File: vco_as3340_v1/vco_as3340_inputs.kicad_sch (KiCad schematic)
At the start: 36 parts, among them J2 FREQ_CV, J3 SOFT_SYNC

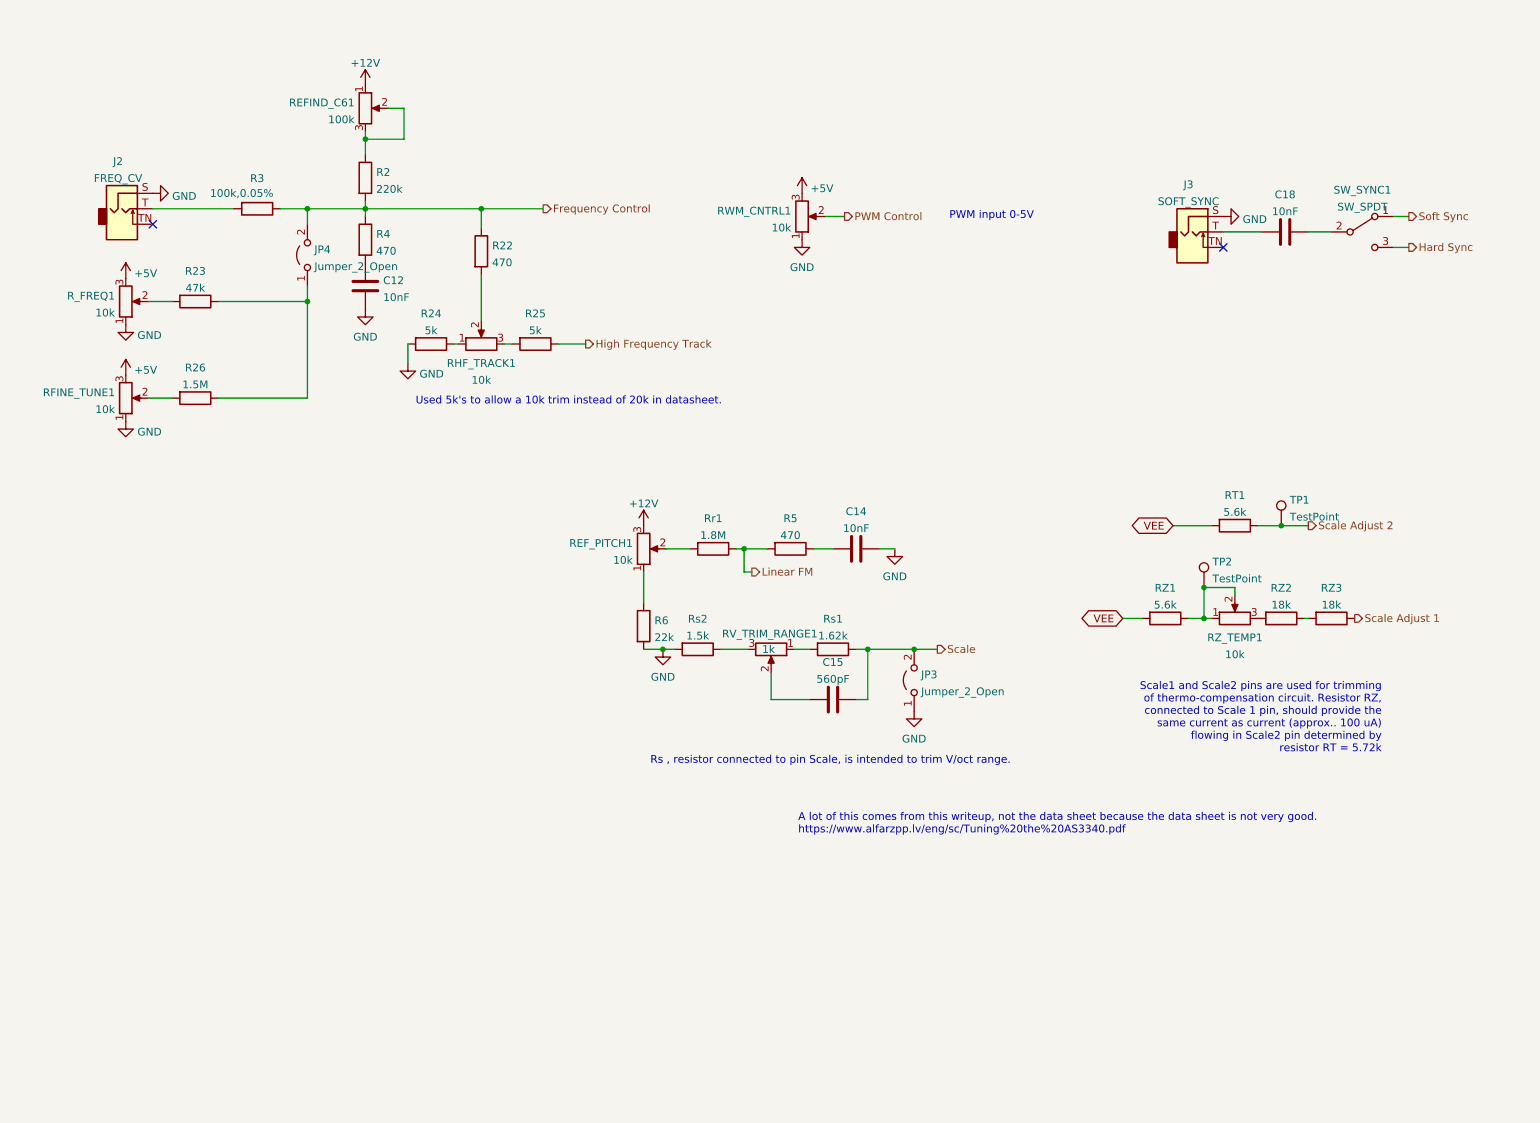
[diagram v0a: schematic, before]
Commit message: Schematic update from breadboarding, start layout
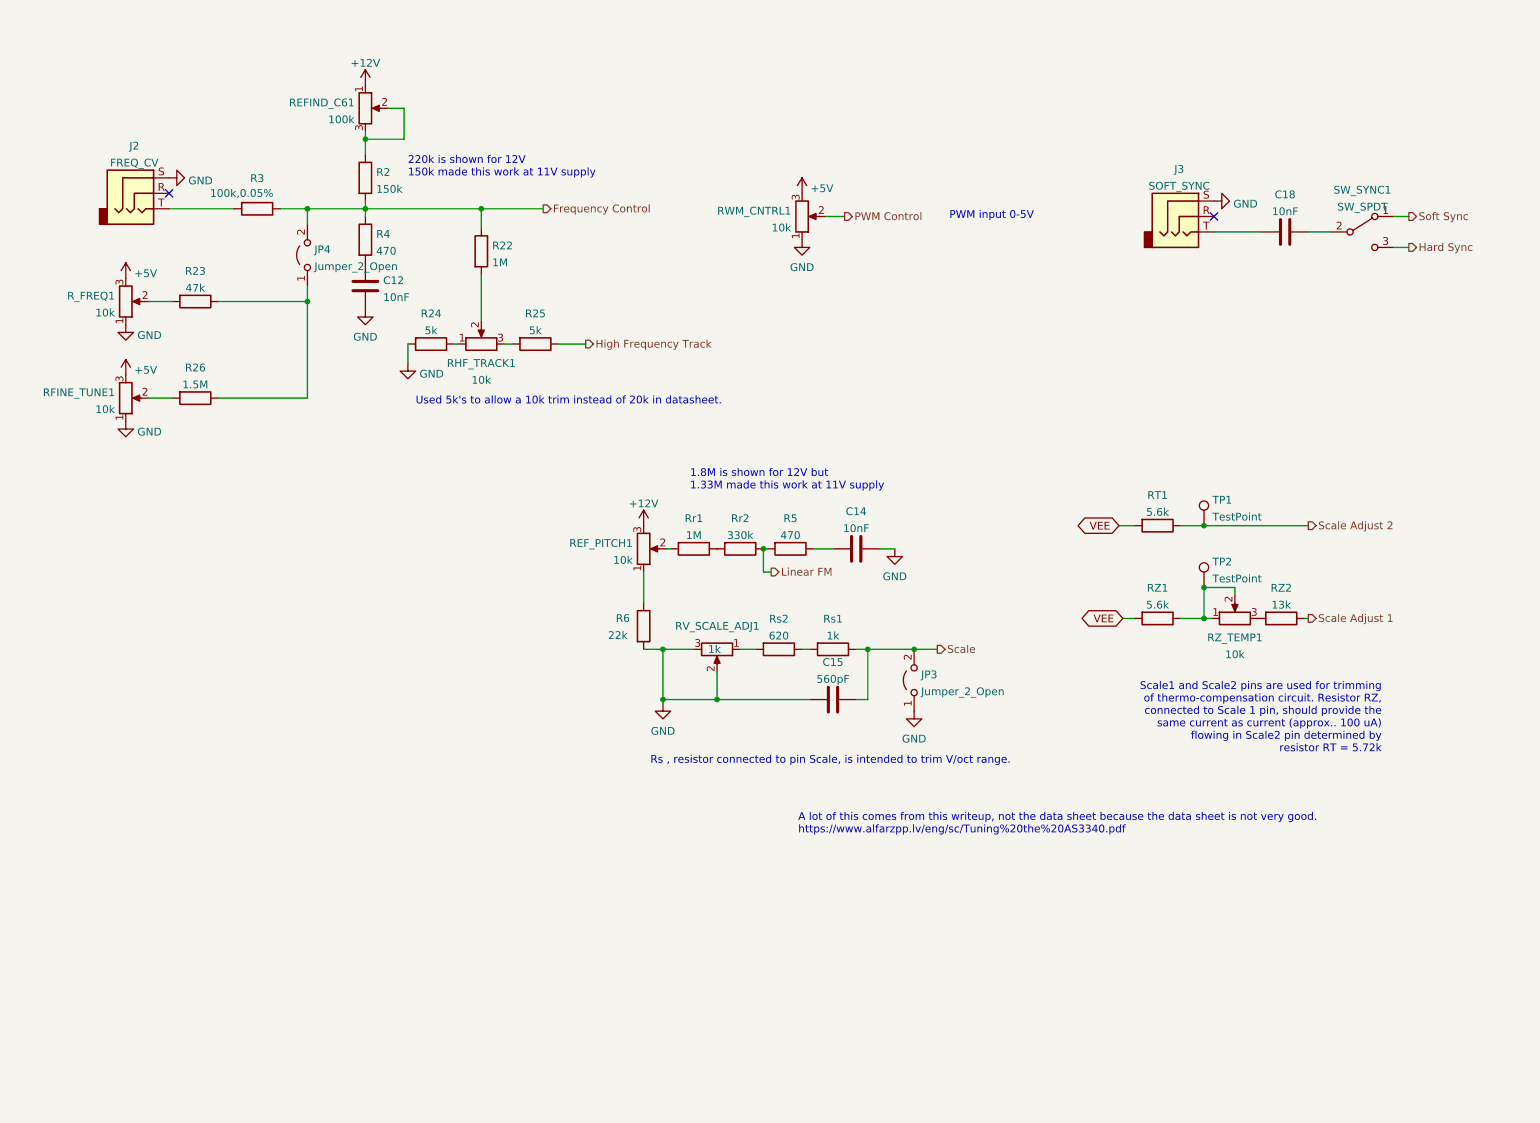
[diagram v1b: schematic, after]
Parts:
- removed RZ3: 18k, Resistor_SMD:R_1206_3216Metric_Pad1.30x1.75mm_HandSolder, symbol Device:R
- added Rr2: 330k, Resistor_SMD:R_1206_3216Metric_Pad1.30x1.75mm_HandSolder, symbol Device:R
- C12, C14, C15, C18: footprint Capacitor_THT:C_Disc_D6.0mm_W4.4mm_P5.00mm -> Capacitor_SMD:C_1206_3216Metric_Pad1.33x1.80mm_HandSolder
- J2, J3: symbol Connector:AudioJack2_SwitchT -> Connector:AudioJack3
- R2: value 220k -> 150k
- R22: value 470 -> 1M
- RZ2: value 18k -> 13k
- Rr1: value 1.8M -> 1M
- Rs1: value 1.62k -> 1k
- Rs2: value 1.5k -> 620
- renumbered RV_TRIM_RANGE1 to RV_SCALE_ADJ1
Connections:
- net GND: now also C15.1, RV_SCALE_ADJ1.2, RV_SCALE_ADJ1.3; no longer Rs2.2
- net Linear FM: now also Rr2.1; no longer Rr1.1
- net Scale Adjust 1: now also RZ2.1
- net at RV_SCALE_ADJ1.1: now also Rs2.2; no longer Rs1.2
- net at Rs2.1: now also Rs1.2; no longer RV_SCALE_ADJ1.3
- new net: Rr1.1, Rr2.2
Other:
- note added: "1.8M is shown for 12V but 1.33M made this work at 11V supply"
- note added: "220k is shown for 12V 150k made this work at 11V supply"
- moved on the sheet: RT1, RV_SCALE_ADJ1, RZ1, Rr1, TP1

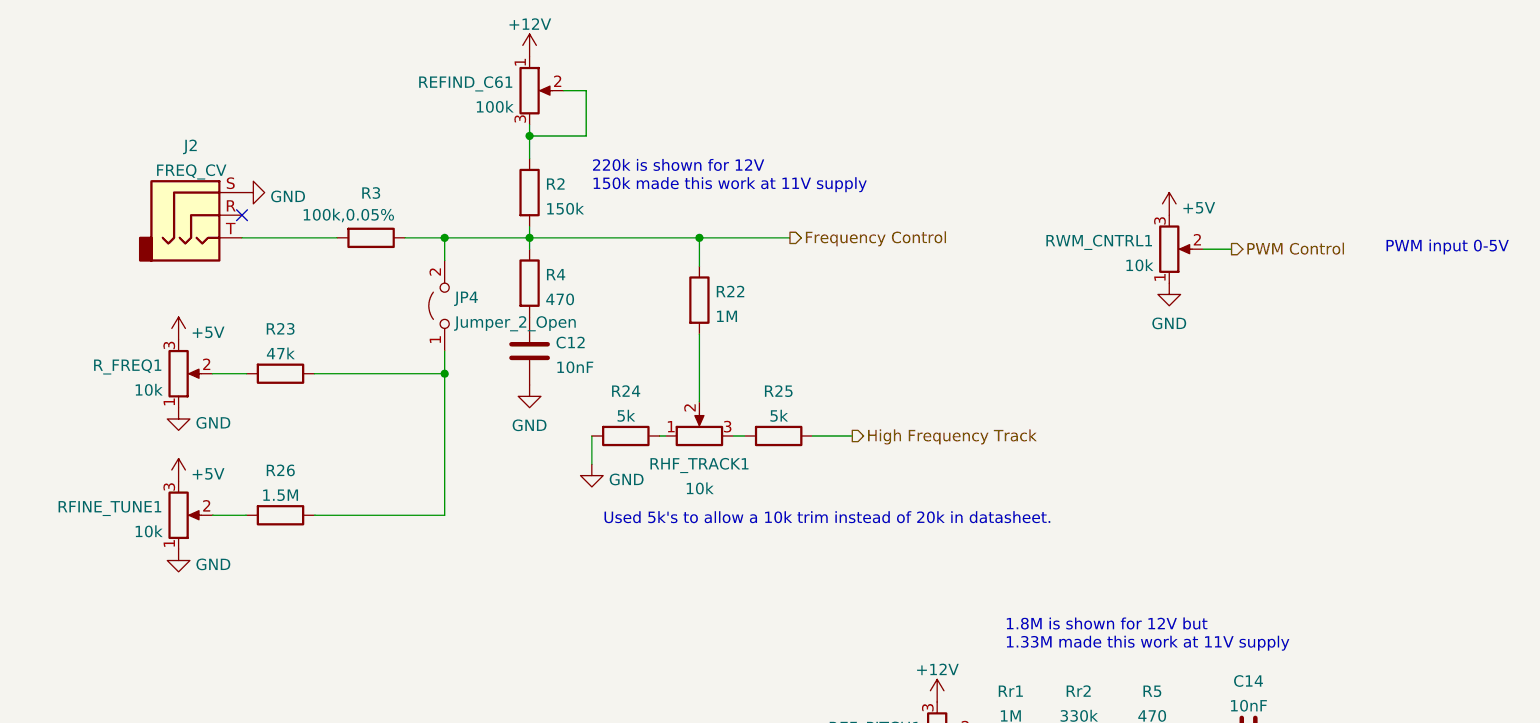
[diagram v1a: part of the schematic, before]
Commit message: Layout and routing done
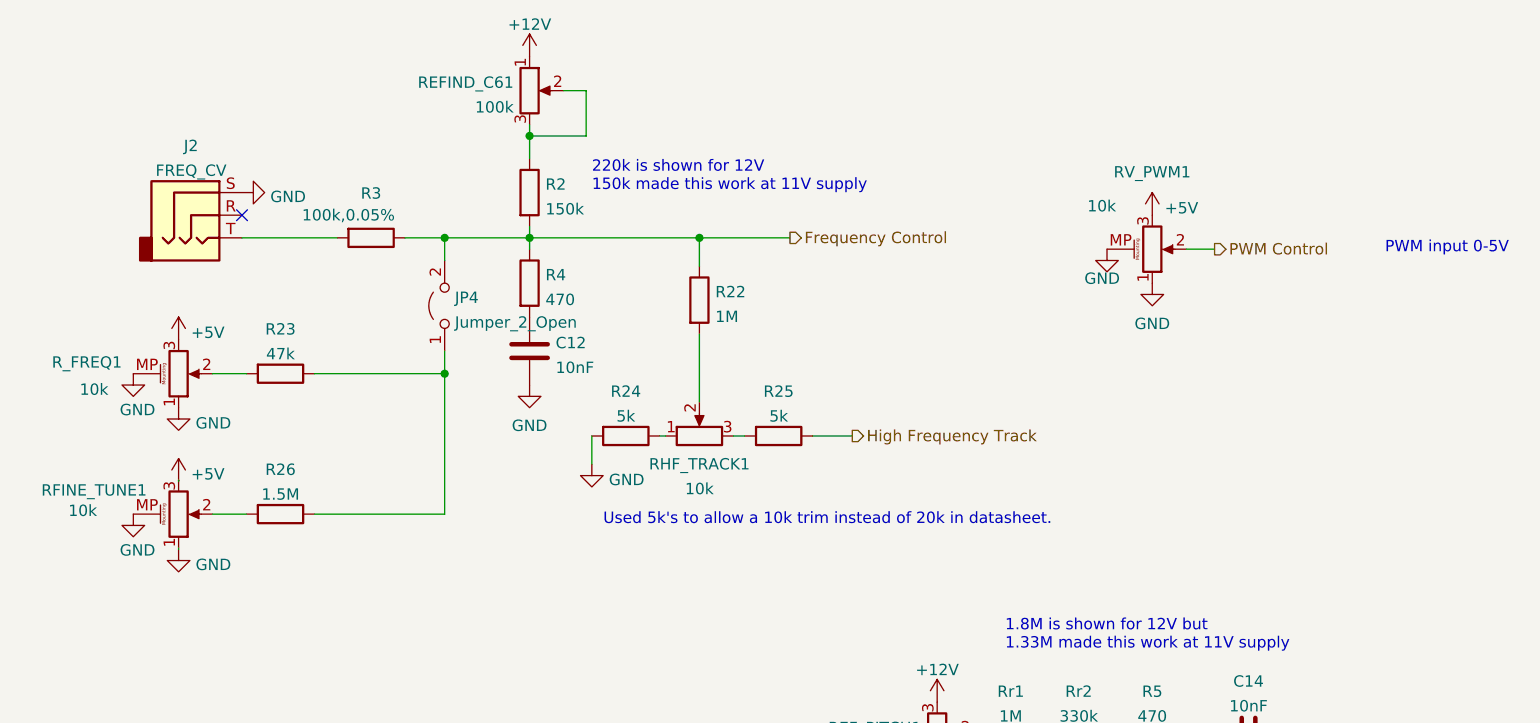
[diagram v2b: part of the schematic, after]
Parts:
- RFINE_TUNE1, R_FREQ1: symbol Device:R_Potentiometer -> Device:R_Potentiometer_MountingPin
- RV_PWM1: renamed from RWM_CNTRL1; symbol Device:R_Potentiometer -> Device:R_Potentiometer_MountingPin
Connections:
- net GND: now also RFINE_TUNE1.MP (MountPin), RV_PWM1.MP (MountPin), R_FREQ1.MP (MountPin)

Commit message: Geographic re-annotate and cleanup
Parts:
- J101: renamed from J3; value SOFT_SYNC -> SYNC
- renumbered C15 to C5, RHF_TRACK1 to HF_TRACK1, J2 to J100, JP4 to JP1, JP3 to JP4, R2 to R1, R5 to R12, R4 to R19, R23 to R2, R25 to R21, R24 to R23, R26 to R3, R3 to R30, R6 to R4, REFIND_C61 to REFIND_C6, RZ2 to RZ1, RZ1 to RZ2, Rr2 to Rr1, Rr1 to Rr2, RV_SCALE_ADJ1 to SCALE_ADJ1, TP2 to TP1, TP1 to TP2
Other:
- note added: "Sync switch from AI Synthesis AI011 design."
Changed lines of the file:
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@@
     (title "3340_VCO")
     (date "2022-07-02")
-    (rev "0.1")
+    (rev "1.0")
     (company "RobotDialogs")
   )
@@
   (text "220k is shown for 12V\n150k made this work at 11V supply"
     (at 76.835 41.91 0)
+    (effects (font (size 1.27 1.27)) (justify left bottom))
+  )
+  (text "Sync switch from AI Synthesis AI011 design." (at 200.914 58.42 0)
     (effects (font (size 1.27 1.27)) (justify left bottom))
   )
@@
   (symbol (lib_id "Device:R") (at 69.85 52.07 0) (unit 1)
     (in_bom yes) (on_board yes) (fields_autoplaced)
-    (property "Reference" "R4" (id 0) (at 71.628 51.1615 0)
+    (property "Reference" "R19" (id 0) (at 71.628 51.1615 0)
       (effects (font (size 1.27 1.27)) (justify left))
     )
@@
   (symbol (lib_id "Device:R") (at 139.7 102.87 270) (unit 1)
     (in_bom yes) (on_board yes) (fields_autoplaced)
-    (property "Reference" "R5" (id 0) (at 139.7 97.8875 90))
+    (property "Reference" "R12" (id 0) (at 139.7 97.8875 90))
     (property "Value" "470" (id 1) (at 139.7 100.6626 90))
     (property "Footprint" "Resistor_SMD:R_1206_3216Metric_Pad1.30x1.75mm_HandSolder" (id 2) (at 139.7 101.092 90)
@@
   (symbol (lib_id "Device:R") (at 123.825 102.87 270) (unit 1)
     (in_bom yes) (on_board yes) (fields_autoplaced)
-    (property "Reference" "Rr1" (id 0) (at 123.825 97.8875 90))
+    (property "Reference" "Rr2" (id 0) (at 123.825 97.8875 90))
     (property "Value" "1M" (id 1) (at 123.825 100.6626 90))
     (property "Footprint" "Resistor_SMD:R_1206_3216Metric_Pad1.30x1.75mm_HandSolder" (id 2) (at 123.825 101.092 90)
@@
   (symbol (lib_id "Device:R") (at 69.85 41.91 0) (unit 1)
     (in_bom yes) (on_board yes) (fields_autoplaced)
-    (property "Reference" "R2" (id 0) (at 71.628 41.0015 0)
+    (property "Reference" "R1" (id 0) (at 71.628 41.0015 0)
       (effects (font (size 1.27 1.27)) (justify left))
     )
@@
   (symbol (lib_id "Device:R") (at 41.91 77.978 270) (unit 1)
     (in_bom yes) (on_board yes) (fields_autoplaced)
-    (property "Reference" "R26" (id 0) (at 41.91 72.9955 90))
+    (property "Reference" "R3" (id 0) (at 41.91 72.9955 90))
     (property "Value" "1.5M" (id 1) (at 41.91 75.7706 90))
     (property "Footprint" "Resistor_SMD:R_1206_3216Metric_Pad1.30x1.75mm_HandSolder" (id 2) (at 41.91 76.2 90)
@@
   (symbol (lib_id "Device:R") (at 52.07 46.99 270) (unit 1)
     (in_bom yes) (on_board yes)
-    (property "Reference" "R3" (id 0) (at 52.07 42.0075 90))
+    (property "Reference" "R30" (id 0) (at 52.07 42.0075 90))
     (property "Value" "100k,0.05%" (id 1) (at 49.53 44.45 90))
     (property "Footprint" "Resistor_SMD:R_1206_3216Metric_Pad1.30x1.75mm_HandSolder" (id 2) (at 52.07 45.212 90)
@@
   (symbol (lib_id "Device:R_Potentiometer") (at 127.635 119.38 270) (unit 1)
     (in_bom yes) (on_board yes)
-    (property "Reference" "RV_SCALE_ADJ1" (id 0) (at 134.62 115.57 90)
+    (property "Reference" "SCALE_ADJ1" (id 0) (at 134.62 115.57 90)
       (effects (font (size 1.27 1.27)) (justify right))
     )
@@
   (symbol (lib_id "Connector:TestPoint") (at 207.645 99.06 0) (unit 1)
     (in_bom yes) (on_board yes) (fields_autoplaced)
-    (property "Reference" "TP1" (id 0) (at 209.042 94.8495 0)
+    (property "Reference" "TP2" (id 0) (at 209.042 94.8495 0)
       (effects (font (size 1.27 1.27)) (justify left))
     )
@@
   (symbol (lib_id "Device:R") (at 41.91 62.23 270) (unit 1)
     (in_bom yes) (on_board yes) (fields_autoplaced)
-    (property "Reference" "R23" (id 0) (at 41.91 57.2475 90))
+    (property "Reference" "R2" (id 0) (at 41.91 57.2475 90))
     (property "Value" "47k" (id 1) (at 41.91 60.0226 90))
     (property "Footprint" "Resistor_SMD:R_1206_3216Metric_Pad1.30x1.75mm_HandSolder" (id 2) (at 41.91 60.452 90)
@@
   (symbol (lib_id "Jumper:Jumper_2_Open") (at 160.02 124.46 90) (unit 1)
     (in_bom yes) (on_board yes) (fields_autoplaced)
-    (property "Reference" "JP3" (id 0) (at 161.163 123.5515 90)
+    (property "Reference" "JP4" (id 0) (at 161.163 123.5515 90)
       (effects (font (size 1.27 1.27)) (justify right))
     )
@@
   (symbol (lib_id "Device:C") (at 146.685 127.635 90) (unit 1)
     (in_bom yes) (on_board yes) (fields_autoplaced)
-    (property "Reference" "C15" (id 0) (at 146.685 121.5095 90))
+    (property "Reference" "C5" (id 0) (at 146.685 121.5095 90))
     (property "Value" "560pF" (id 1) (at 146.685 124.2846 90))
     (property "Footprint" "Capacitor_SMD:C_1206_3216Metric_Pad1.33x1.80mm_HandSolder" (id 2) (at 150.495 126.6698 0)
@@
   (symbol (lib_id "Device:R_Potentiometer") (at 69.85 30.48 0) (unit 1)
     (in_bom yes) (on_board yes) (fields_autoplaced)
-    (property "Reference" "REFIND_C61" (id 0) (at 68.072 29.5715 0)
+    (property "Reference" "REFIND_C6" (id 0) (at 68.072 29.5715 0)
       (effects (font (size 1.27 1.27)) (justify right))
     )
@@
   (symbol (lib_id "Jumper:Jumper_2_Open") (at 60.325 54.61 90) (unit 1)
     (in_bom yes) (on_board yes) (fields_autoplaced)
-    (property "Reference" "JP4" (id 0) (at 61.468 53.7015 90)
+    (property "Reference" "JP1" (id 0) (at 61.468 53.7015 90)
       (effects (font (size 1.27 1.27)) (justify right))
     )
@@
   (symbol (lib_id "Device:R_Potentiometer") (at 88.9 69.215 90) (unit 1)
     (in_bom yes) (on_board yes) (fields_autoplaced)
-    (property "Reference" "RHF_TRACK1" (id 0) (at 88.9 72.3805 90))
+    (property "Reference" "HF_TRACK1" (id 0) (at 88.9 72.3805 90))
     (property "Value" "10k" (id 1) (at 88.9 75.1556 90))
     (property "Footprint" "Potentiometer_THT:Potentiometer_Bourns_3296W_Vertical" (id 2) (at 88.9 69.215 0)
@@
   (symbol (lib_id "Device:R") (at 220.345 114.3 270) (unit 1)
     (in_bom yes) (on_board yes) (fields_autoplaced)
-    (property "Reference" "RZ2" (id 0) (at 220.345 109.3175 90))
+    (property "Reference" "RZ1" (id 0) (at 220.345 109.3175 90))
     (property "Value" "13k" (id 1) (at 220.345 112.0926 90))
     (property "Footprint" "Resistor_SMD:R_1206_3216Metric_Pad1.30x1.75mm_HandSolder" (id 2) (at 220.345 112.522 90)
@@
   (symbol (lib_id "Connector:AudioJack3") (at 204.216 48.26 0) (unit 1)
     (in_bom yes) (on_board yes) (fields_autoplaced)
-    (property "Reference" "J3" (id 0) (at 203.581 40.4835 0))
-    (property "Value" "SOFT_SYNC" (id 1) (at 203.581 43.2586 0))
+    (property "Reference" "J101" (id 0) (at 203.581 40.4835 0))
+    (property "Value" "SYNC" (id 1) (at 203.581 43.2586 0))
     (property "Footprint" "My Stuff:Jack_3.5mm_MJ-355W_Vertical" (id 2) (at 204.216 48.26 0)
       (effects (font (size 1.27 1.27)) hide)
@@
   (symbol (lib_id "Device:R") (at 200.025 114.3 270) (unit 1)
     (in_bom yes) (on_board yes) (fields_autoplaced)
-    (property "Reference" "RZ1" (id 0) (at 200.025 109.3175 90))
+    (property "Reference" "RZ2" (id 0) (at 200.025 109.3175 90))
     (property "Value" "5.6k" (id 1) (at 200.025 112.0926 90))
     (property "Footprint" "Resistor_SMD:R_1206_3216Metric_Pad1.30x1.75mm_HandSolder" (id 2) (at 200.025 112.522 90)
@@
   (symbol (lib_id "Connector:TestPoint") (at 207.645 109.22 0) (unit 1)
     (in_bom yes) (on_board yes) (fields_autoplaced)
-    (property "Reference" "TP2" (id 0) (at 209.042 105.0095 0)
+    (property "Reference" "TP1" (id 0) (at 209.042 105.0095 0)
       (effects (font (size 1.27 1.27)) (justify left))
     )
@@
   (symbol (lib_id "Device:R") (at 97.79 69.215 270) (unit 1)
     (in_bom yes) (on_board yes) (fields_autoplaced)
-    (property "Reference" "R25" (id 0) (at 97.79 64.2325 90))
+    (property "Reference" "R21" (id 0) (at 97.79 64.2325 90))
     (property "Value" "5k" (id 1) (at 97.79 67.0076 90))
     (property "Footprint" "Resistor_SMD:R_1206_3216Metric_Pad1.30x1.75mm_HandSolder" (id 2) (at 97.79 67.437 90)
@@
   (symbol (lib_id "Device:R") (at 80.645 69.215 270) (unit 1)
     (in_bom yes) (on_board yes) (fields_autoplaced)
-    (property "Reference" "R24" (id 0) (at 80.645 64.2325 90))
+    (property "Reference" "R23" (id 0) (at 80.645 64.2325 90))
     (property "Value" "5k" (id 1) (at 80.645 67.0076 90))
     (property "Footprint" "Resistor_SMD:R_1206_3216Metric_Pad1.30x1.75mm_HandSolder" (id 2) (at 80.645 67.437 90)
@@
   (symbol (lib_id "Connector:AudioJack3") (at 32.512 44.45 0) (unit 1)
     (in_bom yes) (on_board yes) (fields_autoplaced)
-    (property "Reference" "J2" (id 0) (at 31.877 36.6735 0))
+    (property "Reference" "J100" (id 0) (at 31.877 36.6735 0))
     (property "Value" "FREQ_CV" (id 1) (at 31.877 39.4486 0))
     (property "Footprint" "My Stuff:Jack_3.5mm_MJ-355W_Vertical" (id 2) (at 32.512 44.45 0)
@@
   (symbol (lib_id "Device:R") (at 115.57 115.57 0) (unit 1)
     (in_bom yes) (on_board yes)
-    (property "Reference" "R6" (id 0) (at 110.998 114.3 0)
+    (property "Reference" "R4" (id 0) (at 110.998 114.3 0)
       (effects (font (size 1.27 1.27)) (justify left))
     )
@@
   (symbol (lib_id "Device:R") (at 131.445 102.87 270) (unit 1)
     (in_bom yes) (on_board yes) (fields_autoplaced)
-    (property "Reference" "Rr2" (id 0) (at 131.445 97.8875 90))
+    (property "Reference" "Rr1" (id 0) (at 131.445 97.8875 90))
     (property "Value" "330k" (id 1) (at 131.445 100.6626 90))
     (property "Footprint" "Resistor_SMD:R_1206_3216Metric_Pad1.30x1.75mm_HandSolder" (id 2) (at 131.445 101.092 90)
